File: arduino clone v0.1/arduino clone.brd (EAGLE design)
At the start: 72.9 x 27.6 mm, 47 parts, among them J203 ICSP HEADER, J402 FTDI Breakout Header, U101 ATMEGA328P_TQFP, U301 CH340G, Y101 16MHz, Y301 12MHz

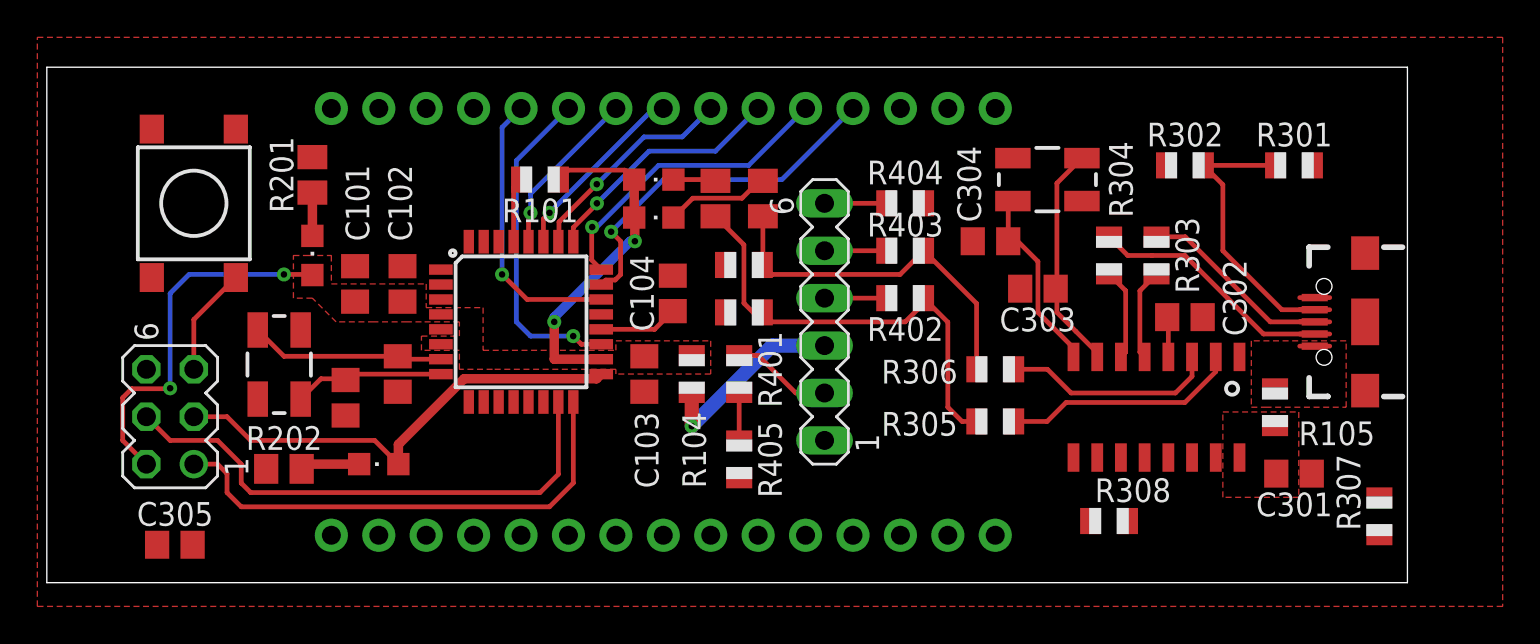
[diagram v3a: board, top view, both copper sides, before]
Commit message: palce and route C305
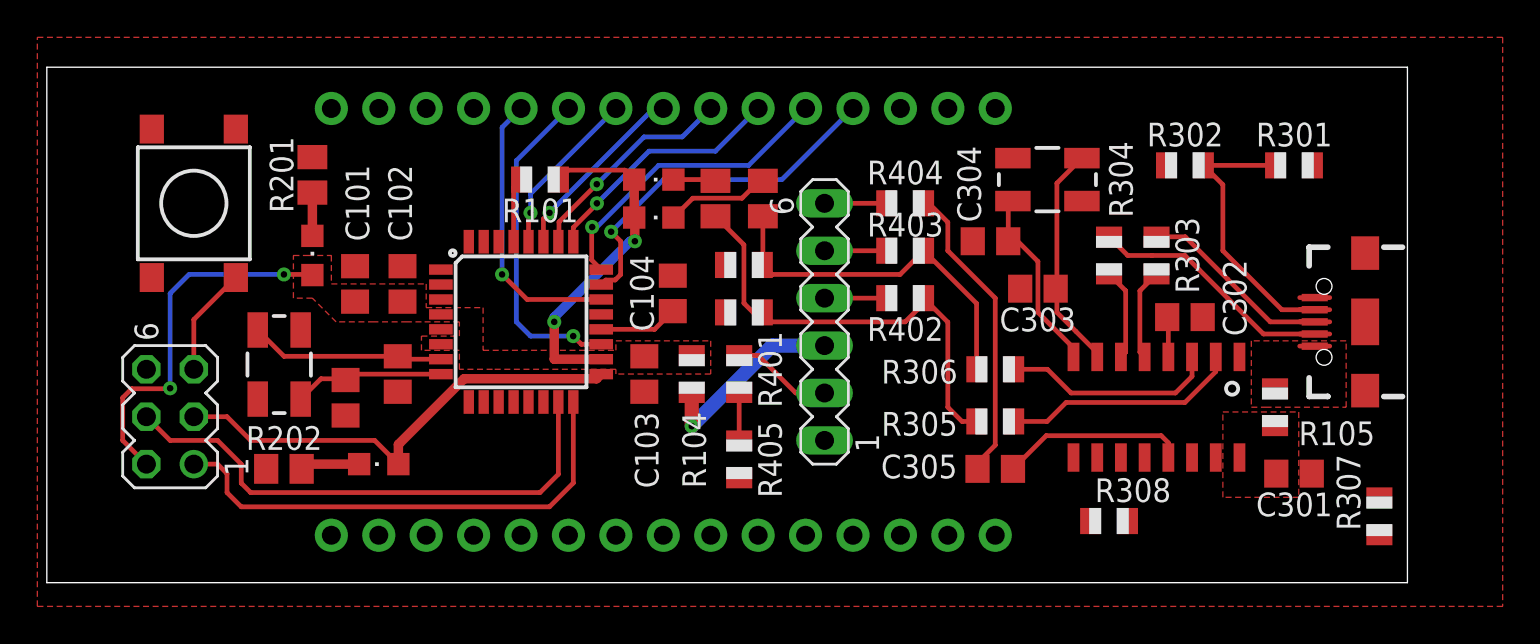
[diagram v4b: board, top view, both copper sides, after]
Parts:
- moved C305 44.1 mm to (59.7, 44.2)
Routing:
- net MCU_RESET: track 9.35 -> 25.7 mm
- net CH340G_DTR: track 0.00 -> 10.0 mm
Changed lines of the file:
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@@
 <attribute name="SPICEPREFIX" value="C" x="59.436" y="56.388" size="1.778" layer="27" rot="R180" display="off"/>
 </element>
-<element name="C305" library="rcl" library_urn="urn:adsk.eagle:library:334" package="C0805" package3d_urn="urn:adsk.eagle:package:23617/2" value="0.1uF" x="15.748" y="40.132" smashed="yes" rot="R180">
-<attribute name="NAME" x="13.716" y="41.148" size="1.27" layer="25"/>
-<attribute name="SPICEPREFIX" value="C" x="15.748" y="40.132" size="1.778" layer="27" rot="R180" display="off"/>
+<element name="C305" library="rcl" library_urn="urn:adsk.eagle:library:334" package="C0805" package3d_urn="urn:adsk.eagle:package:23617/2" value="0.1uF" x="59.69" y="44.196" smashed="yes" rot="R180">
+<attribute name="NAME" x="57.658" y="44.958" size="1.27" layer="25" rot="R180"/>
+<attribute name="SPICEPREFIX" value="C" x="59.69" y="44.196" size="1.778" layer="27" rot="R180" display="off"/>
 </element>
 <element name="J201" library="adafruit" package="1X15-CB" value="" x="41.91" y="40.64" smashed="yes"/>
@@
 <wire x1="34.306" y1="59.69" x2="33.89" y2="59.274" width="0.254" layer="1"/>
 <wire x1="33.89" y1="59.274" x2="33.89" y2="56.3626" width="0.254" layer="1"/>
+<wire x1="58.74" y1="44.196" x2="58.74" y2="44.516" width="0.254" layer="1"/>
+<wire x1="58.74" y1="44.516" x2="59.69" y2="45.466" width="0.254" layer="1"/>
+<wire x1="59.69" y1="45.466" x2="59.69" y2="53.34" width="0.254" layer="1"/>
+<wire x1="57.15" y1="55.88" x2="57.15" y2="57.404" width="0.254" layer="1"/>
+<wire x1="57.15" y1="57.404" x2="56.134" y2="58.42" width="0.254" layer="1"/>
+<wire x1="56.134" y1="58.42" x2="55.864" y2="58.42" width="0.254" layer="1"/>
+<wire x1="59.69" y1="53.34" x2="57.15" y2="55.88" width="0.254" layer="1"/>
 <wire x1="34.306" y1="59.69" x2="55.864" y2="58.42" width="0" layer="19" extent="1-1"/>
 <wire x1="29.21" y1="63.5" x2="33.89" y2="59.274" width="0" layer="19" extent="1-1"/>
 <wire x1="19.014" y1="54.445" x2="29.21" y2="63.5" width="0" layer="19" extent="1-1"/>
-<wire x1="14.798" y1="40.132" x2="16.764" y2="49.53" width="0" layer="19" extent="1-1"/>
-<wire x1="29.21" y1="40.64" x2="14.798" y2="40.132" width="0" layer="19" extent="1-1"/>
+<wire x1="29.21" y1="40.64" x2="16.764" y2="49.53" width="0" layer="19" extent="1-1"/>
 </signal>
 <signal name="MCU_AREF">
@@
 <contactref element="U301" pad="13"/>
 <contactref element="C305" pad="1"/>
-<wire x1="16.698" y1="40.132" x2="68.961" y2="44.803" width="0" layer="19" extent="1-1"/>
+<wire x1="60.64" y1="44.196" x2="62.418" y2="45.974" width="0.254" layer="1"/>
+<wire x1="68.961" y1="45.593" x2="68.961" y2="44.803" width="0.254" layer="1"/>
+<wire x1="62.418" y1="45.974" x2="68.58" y2="45.974" width="0.254" layer="1"/>
+<wire x1="68.58" y1="45.974" x2="68.961" y2="45.593" width="0.254" layer="1"/>
 </signal>
 <signal name="CH340G_CTS">

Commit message: route reset signals
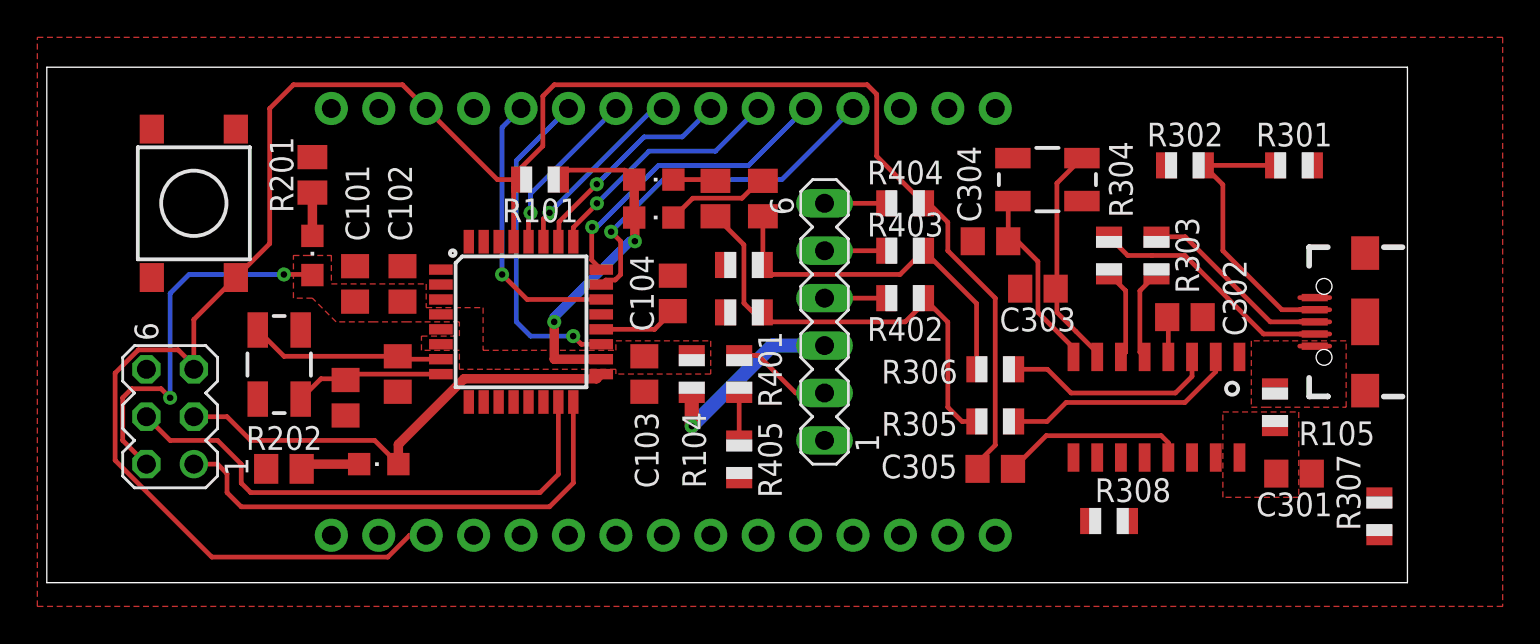
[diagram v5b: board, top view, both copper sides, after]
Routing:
- net MCU_RESET: track 25.7 -> 111.2 mm
- net PP5V0_MCU: track 38.5 -> 39.2 mm
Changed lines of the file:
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@@
 </class>
 </classes>
-<designrules name="default">
+<designrules name="default *">
 <description language="de">&lt;b&gt;EAGLE Design Rules&lt;/b&gt;
 &lt;p&gt;
@@
 <param name="mdViaViaSameLayer" value="6mil"/>
 <param name="mnLayersViaInSmd" value="2"/>
-<param name="mdCopperDimension" value="40mil"/>
+<param name="mdCopperDimension" value="10mil"/>
 <param name="mdDrill" value="6mil"/>
 <param name="mdSmdStop" value="0mil"/>
@@
 <wire x1="23.08" y1="54.61" x2="21.59" y2="54.61" width="0.254" layer="1"/>
 <via x="21.59" y="54.61" extent="1-16" drill="0.35"/>
-<wire x1="13.4366" y1="48.4886" x2="15.4686" y2="48.4886" width="0.254" layer="1"/>
-<wire x1="15.4686" y1="48.4886" x2="15.494" y2="48.514" width="0.254" layer="1"/>
-<via x="15.494" y="48.514" extent="1-16" drill="0.35"/>
-<wire x1="15.494" y1="48.514" x2="15.494" y2="53.594" width="0.254" layer="16"/>
+<wire x1="13.4366" y1="48.4886" x2="15.0114" y2="48.4886" width="0.254" layer="1"/>
+<wire x1="15.494" y1="48.006" x2="15.0114" y2="48.4886" width="0.254" layer="1"/>
+<via x="15.494" y="48.006" extent="1-16" drill="0.35"/>
+<wire x1="15.494" y1="48.006" x2="15.494" y2="53.594" width="0.254" layer="16"/>
 <wire x1="15.494" y1="53.594" x2="16.51" y2="54.61" width="0.254" layer="16"/>
 <wire x1="16.51" y1="54.61" x2="21.59" y2="54.61" width="0.254" layer="16"/>
@@
 <vertex x="8.382" y="36.83"/>
 </polygon>
-<wire x1="72.771" y1="50.193" x2="76.802" y2="53.37" width="0" layer="19" extent="1-1"/>
 </signal>
 <signal name="MCU_RESET">
@@
 <wire x1="56.134" y1="58.42" x2="55.864" y2="58.42" width="0.254" layer="1"/>
 <wire x1="59.69" y1="53.34" x2="57.15" y2="55.88" width="0.254" layer="1"/>
-<wire x1="34.306" y1="59.69" x2="55.864" y2="58.42" width="0" layer="19" extent="1-1"/>
-<wire x1="29.21" y1="63.5" x2="33.89" y2="59.274" width="0" layer="19" extent="1-1"/>
-<wire x1="19.014" y1="54.445" x2="29.21" y2="63.5" width="0" layer="19" extent="1-1"/>
-<wire x1="29.21" y1="40.64" x2="16.764" y2="49.53" width="0" layer="19" extent="1-1"/>
+<wire x1="29.21" y1="63.5" x2="29.337" y2="63.373" width="0.254" layer="1"/>
+<wire x1="29.337" y1="63.373" x2="33.02" y2="59.69" width="0.254" layer="1"/>
+<wire x1="33.02" y1="59.69" x2="34.306" y2="59.69" width="0.254" layer="1"/>
+<wire x1="53.34" y1="60.944" x2="55.864" y2="58.42" width="0.254" layer="1"/>
+<wire x1="52.832" y1="64.77" x2="53.34" y2="64.262" width="0.254" layer="1"/>
+<wire x1="52.832" y1="64.77" x2="36.068" y2="64.77" width="0.254" layer="1"/>
+<wire x1="34.306" y1="60.33963125" x2="34.306" y2="59.69" width="0.254" layer="1"/>
+<wire x1="35.4584" y1="64.1604" x2="35.4584" y2="61.49203125" width="0.254" layer="1"/>
+<wire x1="35.4584" y1="61.49203125" x2="34.306" y2="60.33963125" width="0.254" layer="1"/>
+<wire x1="36.068" y1="64.77" x2="35.4584" y2="64.1604" width="0.254" layer="1"/>
+<wire x1="53.34" y1="64.262" x2="53.34" y2="60.944" width="0.254" layer="1"/>
+<wire x1="19.014" y1="54.445" x2="20.828" y2="56.259" width="0.254" layer="1"/>
+<wire x1="20.828" y1="63.5" x2="22.098" y2="64.77" width="0.254" layer="1"/>
+<wire x1="22.098" y1="64.77" x2="27.94" y2="64.77" width="0.254" layer="1"/>
+<wire x1="27.94" y1="64.77" x2="29.337" y2="63.373" width="0.254" layer="1"/>
+<wire x1="20.828" y1="56.259" x2="20.828" y2="63.5" width="0.254" layer="1"/>
+<wire x1="13.7926375" y1="50.5714" x2="15.9253625" y2="50.5714" width="0.254" layer="1"/>
+<wire x1="29.21" y1="40.64" x2="28.32236875" y2="40.64" width="0.254" layer="1"/>
+<wire x1="28.32236875" y1="40.64" x2="27.15396875" y2="39.4716" width="0.254" layer="1"/>
+<wire x1="12.5476" y1="44.6536375" x2="12.5476" y2="49.3263625" width="0.254" layer="1"/>
+<wire x1="12.5476" y1="49.3263625" x2="13.7926375" y2="50.5714" width="0.254" layer="1"/>
+<wire x1="27.15396875" y1="39.4716" x2="17.7296375" y2="39.4716" width="0.254" layer="1"/>
+<wire x1="17.7296375" y1="39.4716" x2="12.5476" y2="44.6536375" width="0.254" layer="1"/>
+<wire x1="15.9253625" y1="50.5714" x2="16.764" y2="49.7327625" width="0.254" layer="1"/>
+<wire x1="16.764" y1="49.7327625" x2="16.764" y2="49.53" width="0.254" layer="1"/>
 </signal>
 <signal name="MCU_AREF">
@@
 <wire x1="47.752" y1="50.8" x2="50.546" y2="50.8" width="0.762" layer="16"/>
 <wire x1="76.802" y1="50.77" x2="76.692" y2="60.452" width="0" layer="19" extent="1-1"/>
-<wire x1="74.676" y1="48.498" x2="76.802" y2="50.77" width="0" layer="19" extent="1-1"/>
 <wire x1="57.15" y1="63.5" x2="76.692" y2="60.452" width="0" layer="19" extent="1-1"/>
 <wire x1="50.546" y1="50.8" x2="57.15" y2="63.5" width="0" layer="19" extent="1-1"/>

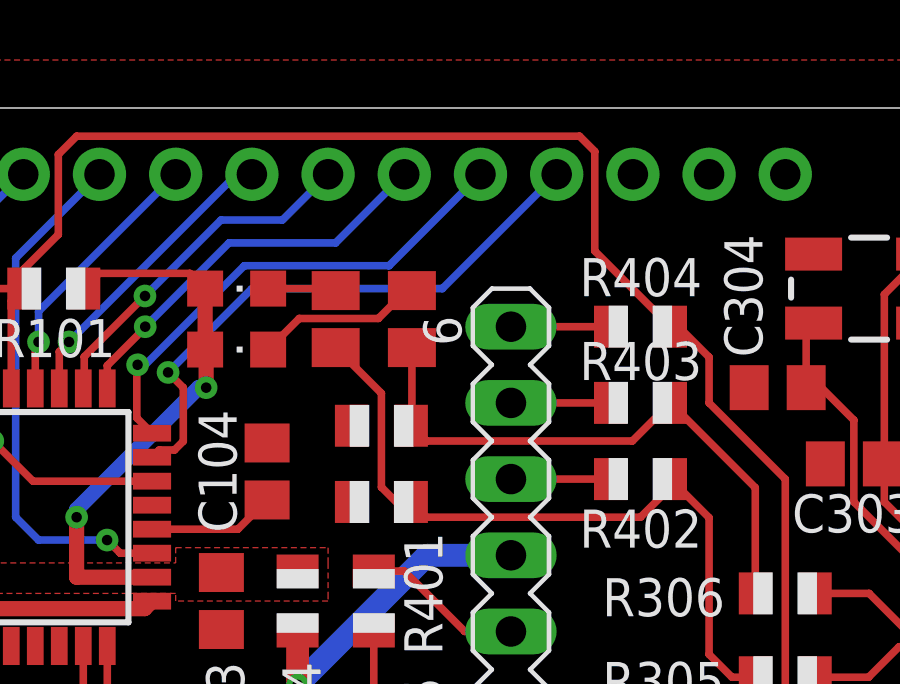
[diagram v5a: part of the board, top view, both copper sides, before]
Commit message: route MCU_AREF
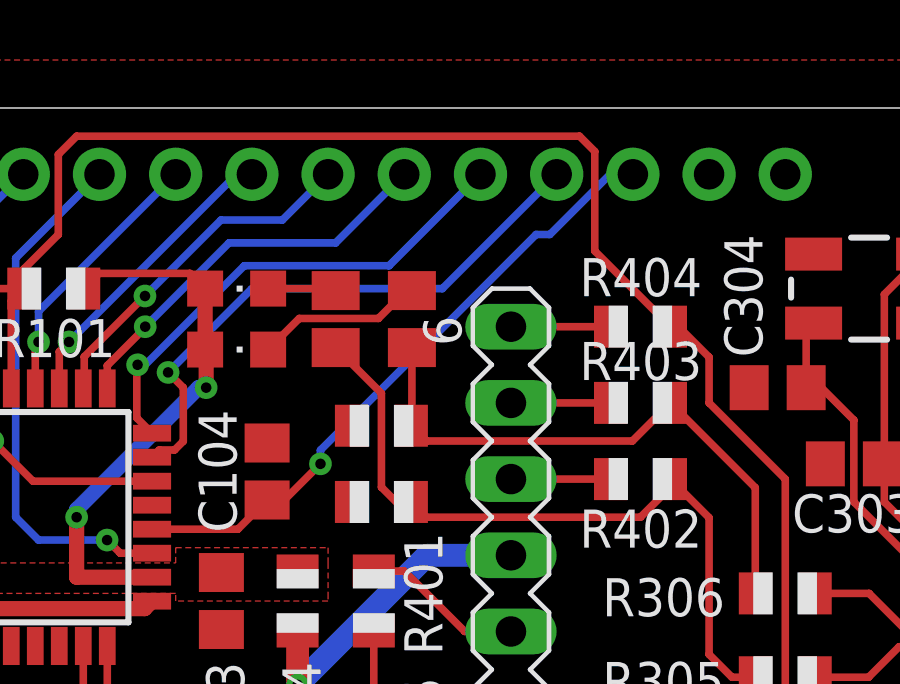
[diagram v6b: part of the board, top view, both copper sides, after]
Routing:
- net MCU_AREF: track 4.24 -> 21.2 mm, vias 0 -> 1
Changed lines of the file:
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@@
 <wire x1="38.5826" y1="51.67" x2="41.444" y2="51.67" width="0.254" layer="1"/>
 <wire x1="41.444" y1="51.67" x2="42.418" y2="52.644" width="0.254" layer="1"/>
-<wire x1="42.418" y1="52.644" x2="54.61" y2="63.5" width="0" layer="19" extent="1-1"/>
+<wire x1="42.418" y1="52.644" x2="42.992" y2="52.644" width="0.254" layer="1"/>
+<wire x1="42.992" y1="52.644" x2="44.196" y2="53.848" width="0.254" layer="1"/>
+<via x="44.196" y="53.848" extent="1-16" drill="0.35"/>
+<wire x1="53.848" y1="63.5" x2="54.61" y2="63.5" width="0.254" layer="16"/>
+<wire x1="44.196" y1="54.3047625" x2="51.3846375" y2="61.4934" width="0.254" layer="16"/>
+<wire x1="51.3846375" y1="61.4934" x2="51.8414" y2="61.4934" width="0.254" layer="16"/>
+<wire x1="51.8414" y1="61.4934" x2="53.848" y2="63.5" width="0.254" layer="16"/>
+<wire x1="44.196" y1="53.848" x2="44.196" y2="54.3047625" width="0.254" layer="16"/>
 </signal>
 <signal name="MCU_D1">
@@
 <contactref element="U101" pad="1"/>
 <contactref element="J201" pad="6"/>
-<wire x1="36.83" y1="40.64" x2="29.9974" y2="54.87" width="0" layer="19" extent="1-1"/>
+<wire x1="29.9974" y1="54.87" x2="36.83" y2="40.64" width="0" layer="19" extent="1-1"/>
 </signal>
 <signal name="MCU_D4">
 <contactref element="U101" pad="2"/>
 <contactref element="J201" pad="7"/>
-<wire x1="39.37" y1="40.64" x2="29.9974" y2="54.07" width="0" layer="19" extent="1-1"/>
+<wire x1="29.9974" y1="54.07" x2="39.37" y2="40.64" width="0" layer="19" extent="1-1"/>
 </signal>
 <signal name="MCU_D5">
@@
 <wire x1="19.812" y1="45.72" x2="26.45" y2="45.72" width="0.254" layer="1"/>
 <wire x1="16.764" y1="46.99" x2="18.542" y2="46.99" width="0.254" layer="1"/>
-<wire x1="38.5826" y1="49.27" x2="59.69" y2="63.5" width="0" layer="19" extent="1-1"/>
+<wire x1="59.69" y1="63.5" x2="38.5826" y2="49.27" width="0" layer="19" extent="1-1"/>
 </signal>
 <signal name="MCU_RX">
